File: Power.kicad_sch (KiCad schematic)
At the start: 78 parts, among them J3 DBT50G-9.5-2P, J38 2.54-1*4, J4 DBT50G-9.5-2P, J5 DBT50G-9.5-2P, J6 DBT50G-9.5-2P, U12 INA226, U13 INA226, U14 INA226, U15 INA226, U5 TPS63070RNMR

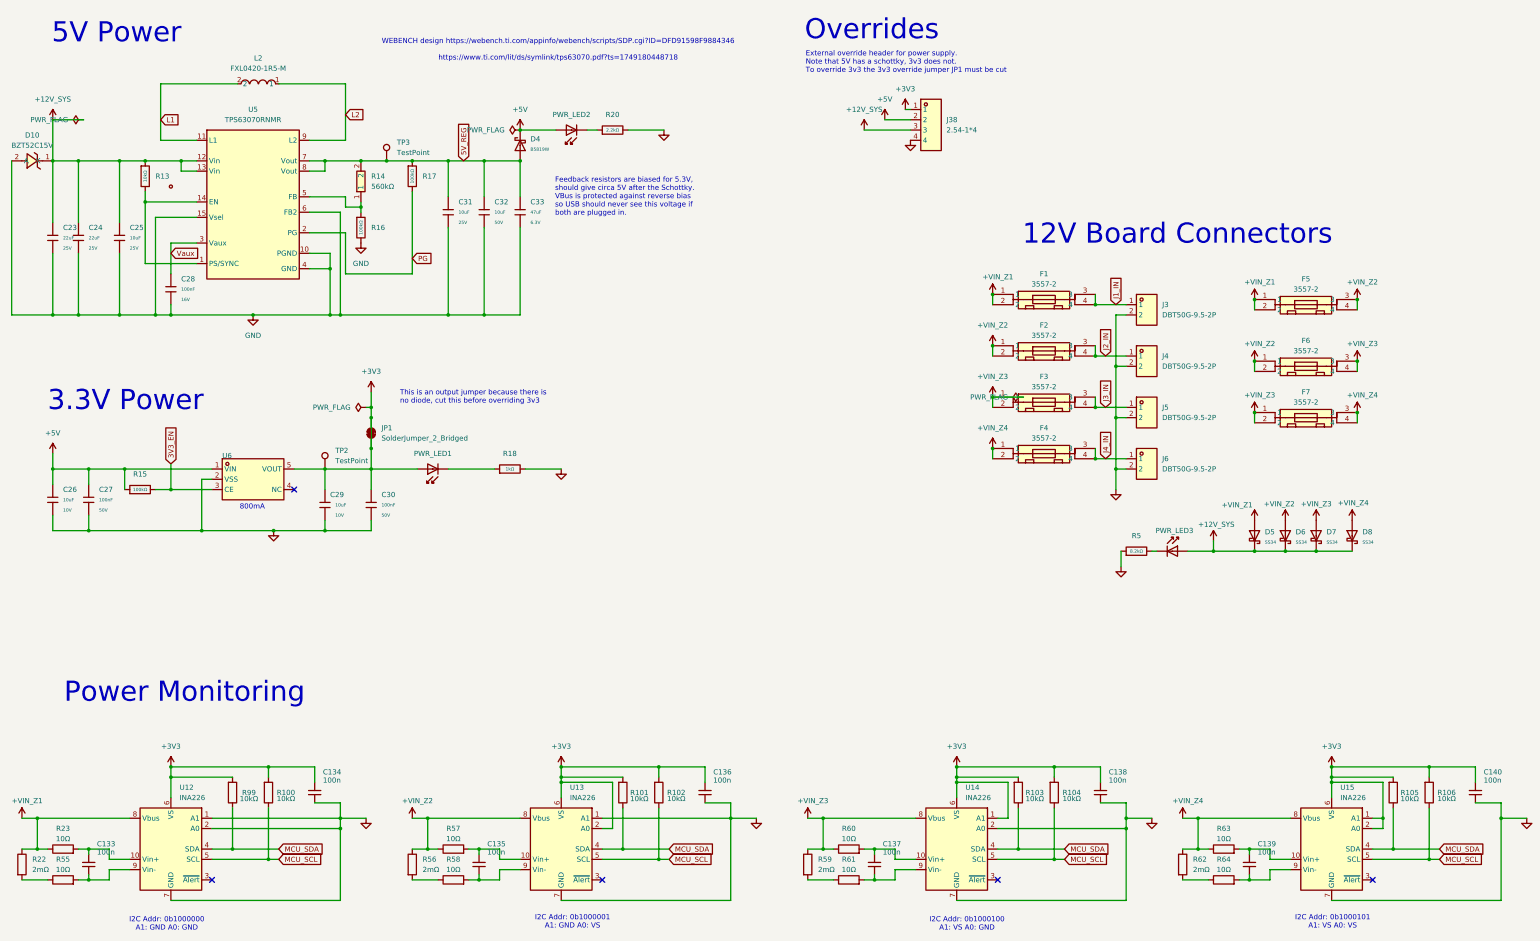
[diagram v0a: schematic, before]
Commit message: Removed power monitoring, it's too much, eh?
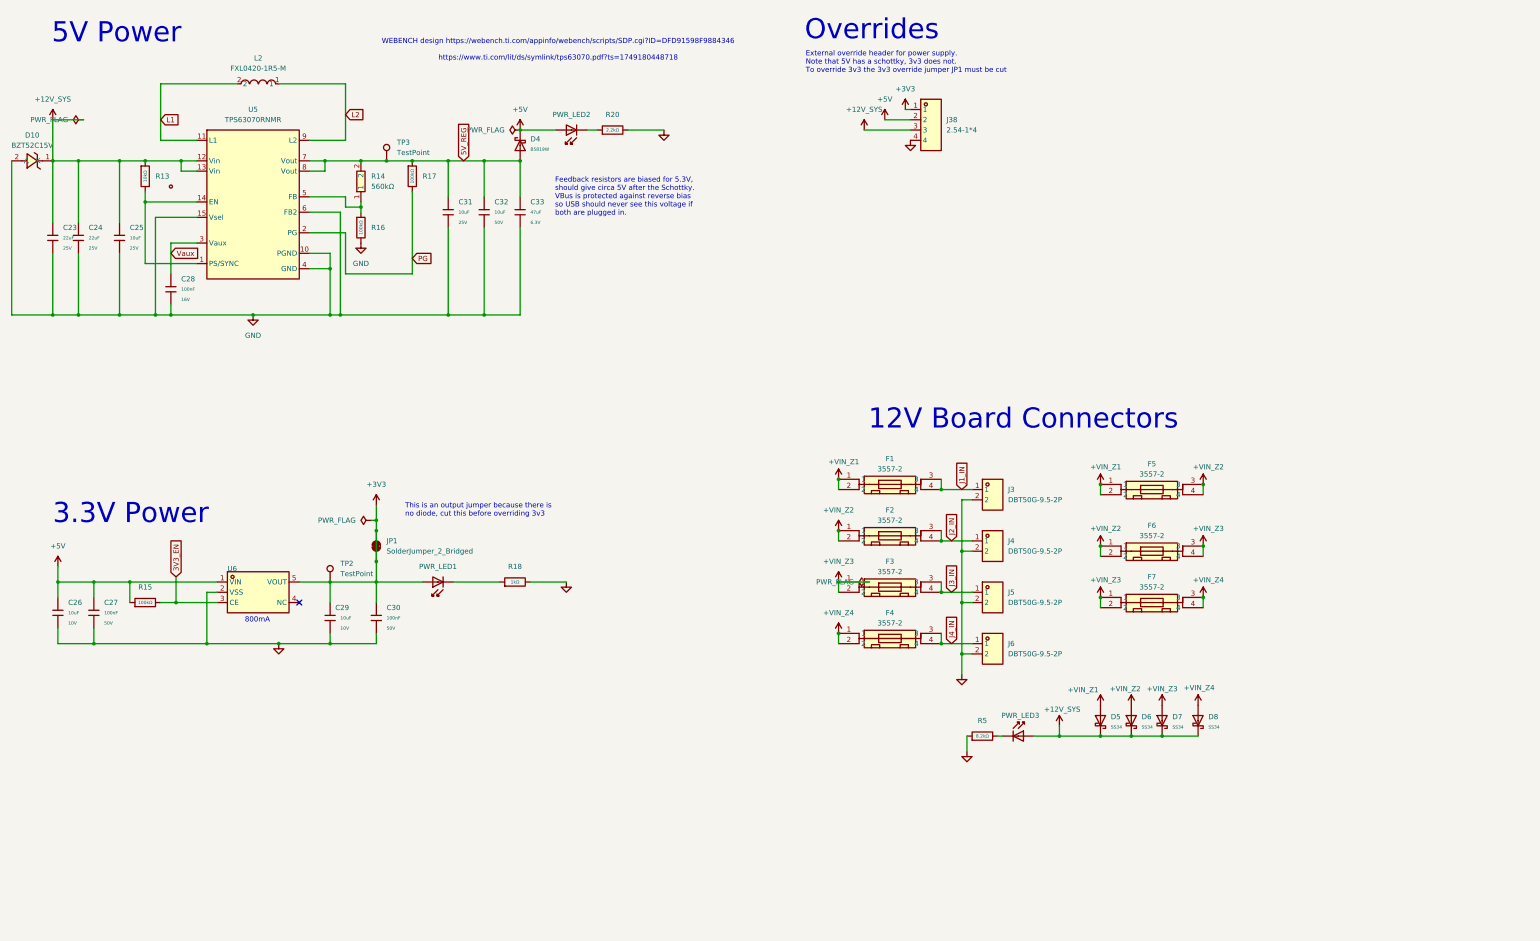
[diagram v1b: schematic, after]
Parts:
- removed C133, C134, C135, C136, C137, C138, C139, C140: 100n, RPI_COMPILED:generic_capc1005x50, symbol RPI_DB:Capacitors | MLCC | M1005/RP-01BJ9Y-KRGF41
- removed R100, R101, R102, R103, R104, R105, R106, R99: 10kΩ, PixelBlit:R_0603, symbol PixelBlit:0603,10kΩ
- removed R22, R56, R59, R62: 2mΩ, Resistor_SMD:R_Shunt_Vishay_WSK2512_6332Metric_T1.19mm, symbol Device:R
- removed R23, R55, R57, R58, R60, R61, R63, R64: 10Ω, PixelBlit:R_0402, symbol Device:R
- removed U12, U13, U14, U15: INA226, Package_SO:TSSOP-10_3x3mm_P0.5mm, symbol Sensor_Energy:INA226
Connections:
- no-connect marks 5 -> 1
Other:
- note removed: "I2C Addr: 0b1000000 A1: GND A0: GND"
- note removed: "I2C Addr: 0b1000001 A1: GND A0: VS"
- note removed: "I2C Addr: 0b1000100 A1: VS A0: GND"
- note removed: "I2C Addr: 0b1000101 A1: VS A0: VS"
- note removed: "Power Monitoring"
- moved on the sheet: C26, C27, C29, C30, D5, D6, D7, D8, F1, F2, F3, F4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
